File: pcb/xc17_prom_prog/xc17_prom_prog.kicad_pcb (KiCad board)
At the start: 2 copper layers, 123 x 95 mm, 288 parts, among them J1 Conn_02x02_Odd_Even, J2 USB_B_Micro, J3 Conn_02x20_Odd_Even, Q1 BC850, Q10 BC850, Q11 IRLML9301, Q12 IRLML9301, Q13 IRLML9301, Q14 IRLML9301, Q15 BC850, Q16 IRLML9301, Q17 IRLML9301, Q18 IRLML9301, Q19 IRLML9301, Q2 BC850, Q20 BC850, Q21 BC850, Q22 BC850, Q23 BC850, Q24 BC850, Q3 IRLML9301, Q4 IRLML9301, Q5 IRLML9301, Q6 BC850, Q7 IRLML9301, Q8 IRLML9301, Q9 BC850, U1 W25Q32JVSSIM, U10 LM317, U11 LM317, U12 LM317, U13 MC33063AD, U14 MC33063AD, U15 SN74LVC8T245, U16 SN74LVC8T245, U17 SN74LVC8T245, U18 XC17xxx, U2 LT3030, U3 ICE40HX1K-VQ100, U4 93LC56B, U5 FT2232HL, U6 LM317, U7 LM317, U8 LM317, U9 LM317, X1 12M

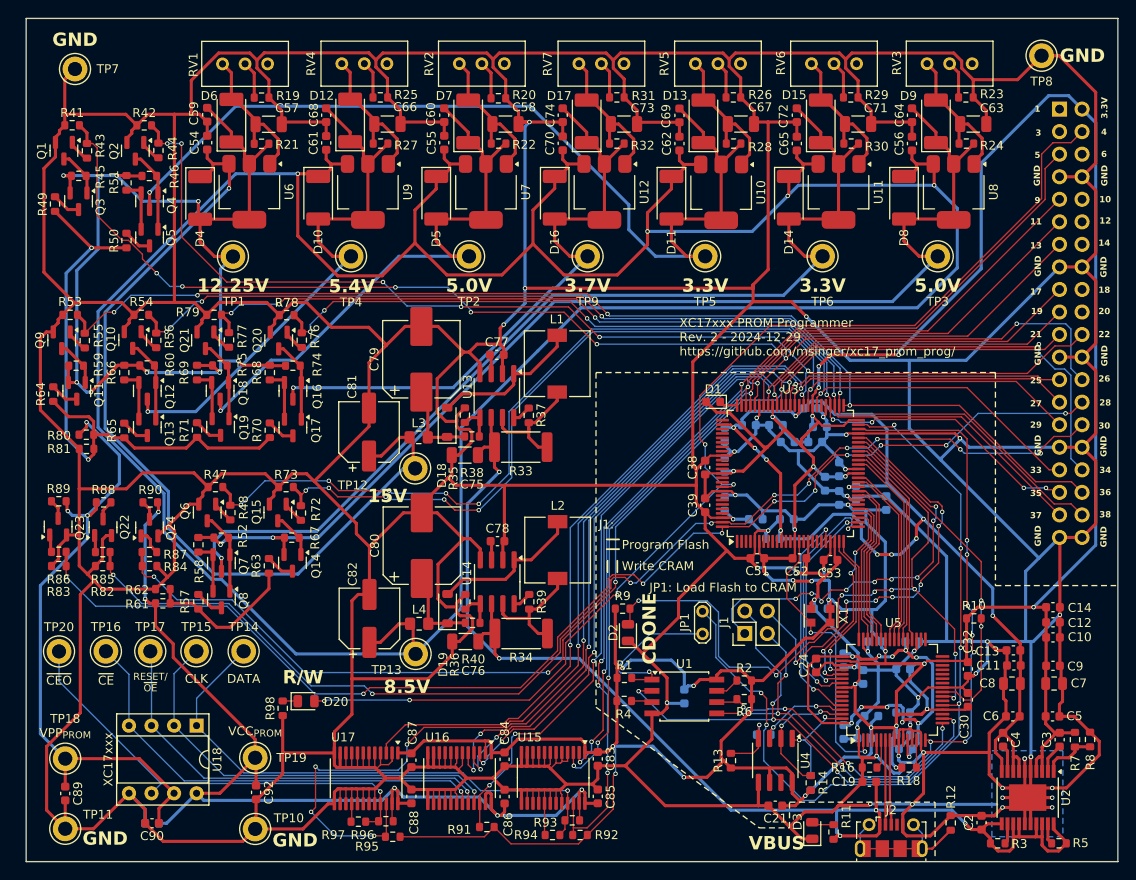
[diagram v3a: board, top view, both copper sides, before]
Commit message: Remove unused components
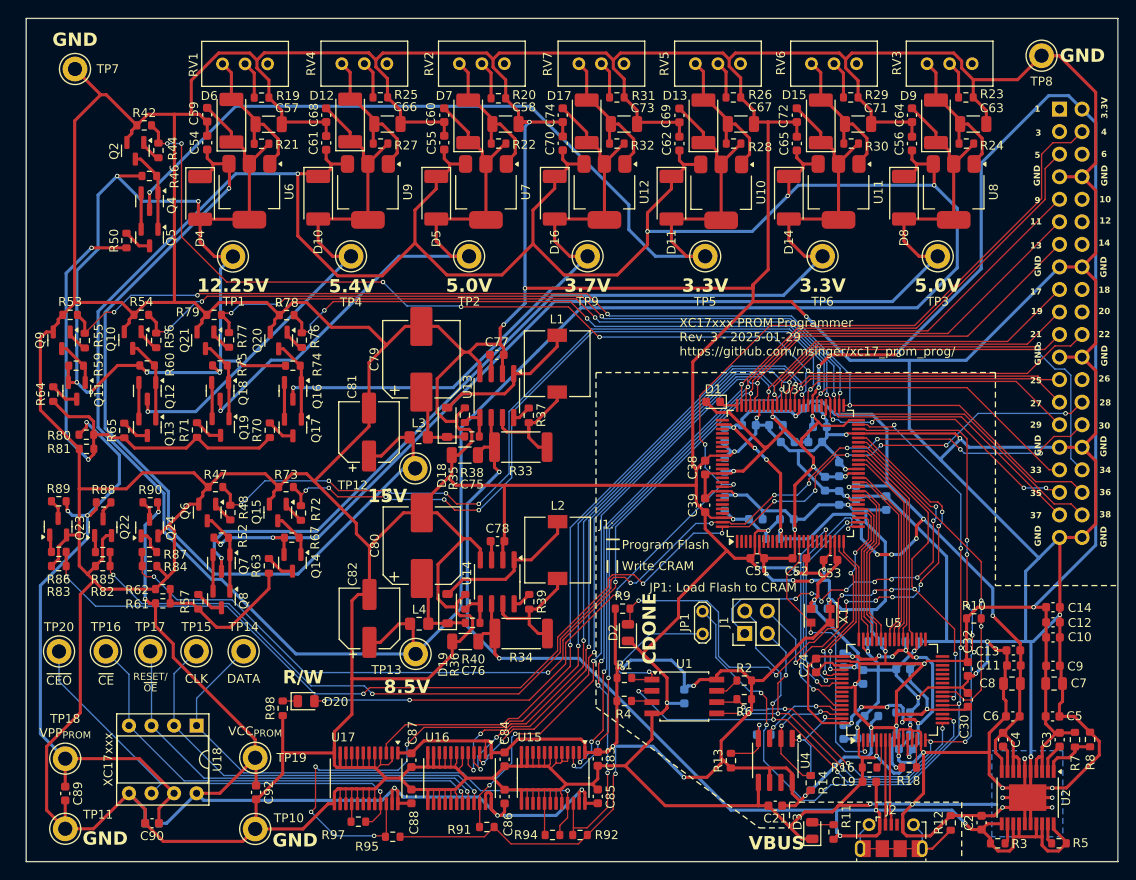
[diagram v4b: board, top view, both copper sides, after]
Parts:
- removed Q1: BC850, Package_TO_SOT_SMD:SOT-23
- removed Q3: IRLML9301, Package_TO_SOT_SMD:SOT-23
- removed R41: 10k, Resistor_SMD:R_0603_1608Metric
- removed R43: 422, Resistor_SMD:R_0603_1608Metric
- removed R45: 2.05k, Resistor_SMD:R_0603_1608Metric
- removed R49: 1.5, Resistor_SMD:R_0603_1608Metric
- removed R51, R58, R66, R68, R69: 1M, Resistor_SMD:R_0603_1608Metric
- removed R93, R96: 100k, Resistor_SMD:R_0603_1608Metric
- R64: value 0 -> 1.5
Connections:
- J3 pad 26: /FPGA/SELECT_VPP_12V25_WEAK -> unconnected-(J3-Pin_26-Pad26)
- U3 pad 69: /FPGA/SELECT_VPP_12V25_WEAK -> unconnected-(U3B-IOR_68-Pad69)
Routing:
- net /FPGA/SELECT_VPP_12V25_WEAK: track 142.6 -> 0.00 mm, vias 7 -> 0
- net +12V25P: track 124.4 -> 114.5 mm, vias 8 -> 7
- net Net-(R50-Pad2): track 67.8 -> 62.0 mm
- net Net-(Q1-C): track 5.25 -> 0.00 mm
- net VCC_{PROM}: track 119.4 -> 115.5 mm
- net GND: track 1606.1 -> 1602.5 mm
- net Net-(Q3-D): track 3.25 -> 0.00 mm
- net Net-(Q1-B): track 2.58 -> 0.00 mm
- net +5VC: track 131.1 -> 129.4 mm
- net Net-(Q4-S): track 5.84 -> 4.10 mm
- net Net-(Q16-S): track 5.85 -> 4.12 mm
- net Net-(Q18-S): track 5.78 -> 4.10 mm
- net Net-(Q12-S): track 5.78 -> 4.10 mm
- net Net-(Q7-S): track 5.73 -> 4.10 mm

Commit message: Migrate from HX1K to HX4K FPGA
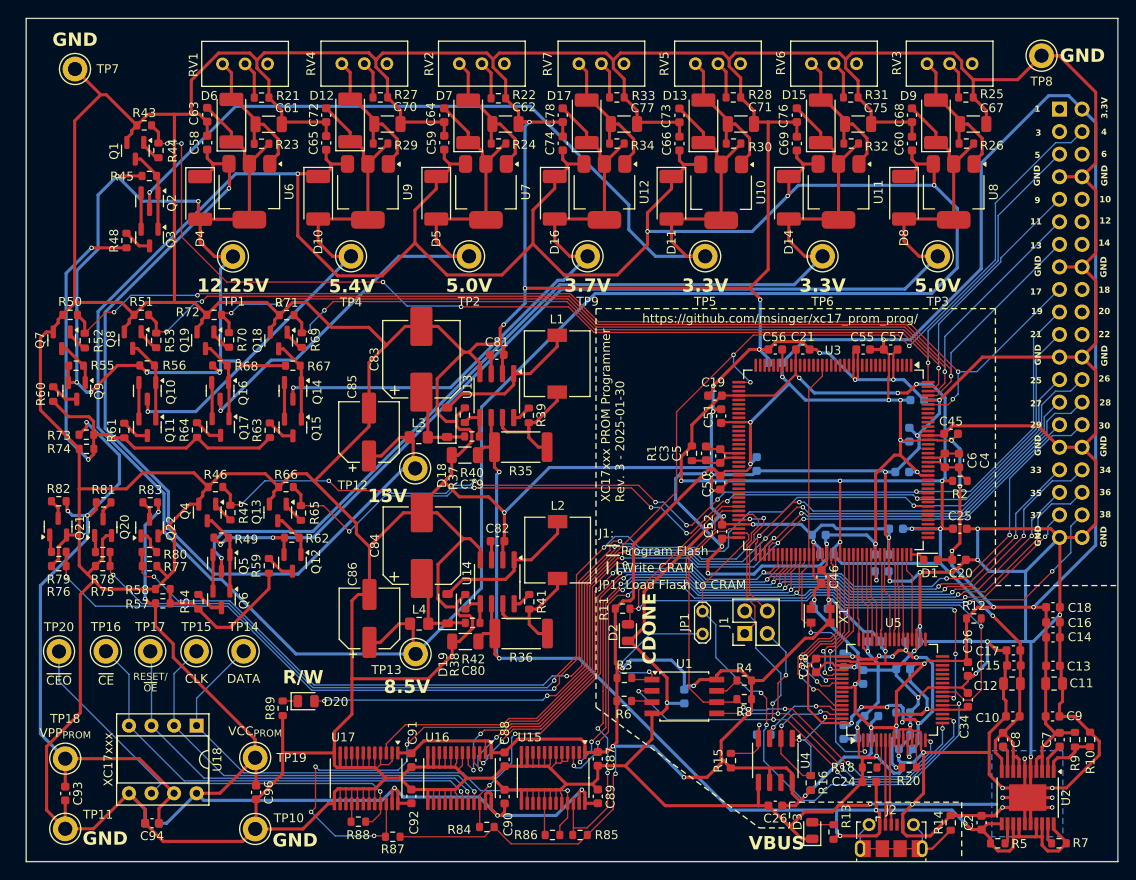
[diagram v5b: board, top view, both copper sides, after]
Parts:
- removed the C15 at (174.1, 98.6)
- removed the C16 at (175.7, 96.4)
- removed the C17 at (183.5, 93.5)
- removed the C18 at (178.4, 83.9)
- removed the C38 at (166.5, 90.6)
- removed the C39 at (166.5, 94.8)
- removed the C40 at (168.7, 90.3)
- removed the C41 at (168.7, 94.7)
- added C19: 100n, Capacitor_SMD:C_0603_1608Metric, F.Cu at (167.6, 82.5)
- added C21: 100n, Capacitor_SMD:C_0603_1608Metric, F.Cu at (177.5, 77.3)
- added C22: 100n, Capacitor_SMD:C_0603_1608Metric, B.Cu at (180.2, 100.4)
- added C25: 10n, Capacitor_SMD:C_0603_1608Metric, F.Cu at (195.2, 97.5)
- added C3: 10µ, Capacitor_SMD:C_0603_1608Metric, F.Cu at (166.6, 89.0)
- added C4: 10µ, Capacitor_SMD:C_0603_1608Metric, F.Cu at (195.1, 89.8)
- added C5: 100n, Capacitor_SMD:C_0603_1608Metric, F.Cu at (168.2, 89.3)
- added C54: 100n, Capacitor_SMD:C_0603_1608Metric, B.Cu at (174.4, 78.8)
- added C55: 100n, Capacitor_SMD:C_0603_1608Metric, F.Cu at (184.3, 77.3)
- added C56: 100n, Capacitor_SMD:C_0603_1608Metric, F.Cu at (174.4, 77.3)
- added C57: 100n, Capacitor_SMD:C_0603_1608Metric, F.Cu at (187.4, 77.3)
- added C6: 100n, Capacitor_SMD:C_0603_1608Metric, F.Cu at (193.5, 89.8)
- added R1: 100, Resistor_SMD:R_0603_1608Metric, F.Cu at (165.0, 89.0)
- added R2: 100, Resistor_SMD:R_0603_1608Metric, F.Cu at (195.2, 92.1)
- C20: value 100n -> 10n; moved to F.Cu
- C23: value 10n -> 100n
- C45, C46, C50: moved to F.Cu
- C53: moved to B.Cu
- U3: value ICE40HX1K-VQ100 -> ICE40HX4K-TQ144; footprint Package_QFP:VQFP-100_14x14mm_P0.5mm -> Package_QFP:TQFP-144_20x20mm_P0.5mm
- moved D1 30.3 mm to (191.9, 101.0), turned to 0 degrees
- moved C20 29.9 mm to (195.1, 101.0), turned to 0 degrees
- moved C23 20.3 mm to (188.0, 97.5), turned to 180 degrees
- moved C51 16.5 mm to (168.3, 84.8), turned to 90 degrees
- moved C45 15.3 mm to (194.2, 86.8), turned to 180 degrees
- moved C43 15.1 mm to (189.5, 86.9), turned to 90 degrees
- moved C53 13.7 mm to (172.3, 90.2), turned to -90 degrees
- moved C44 13.3 mm to (188.7, 91.1)
- moved C46 12.3 mm to (179.6, 102.9), turned to -90 degrees
- moved C48 11.8 mm to (186.4, 102.3), turned to 0 degrees
- moved C42 11.4 mm to (190.4, 83.0)
- moved C52 9.23 mm to (168.4, 97.8), turned to 90 degrees
- moved C49 5.82 mm to (186.4, 100.4), turned to 0 degrees
- moved C50 5.75 mm to (168.2, 92.3), turned to -90 degrees
- moved U3 5.08 mm to (180.9, 89.7), turned to -90 degrees
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- renumbered C6 to C10, C7 to C11, C8 to C12, C9 to C13, C10 to C14, C11 to C15, C12 to C16, C13 to C17, C14 to C18, C19 to C24, C21 to C26, C22 to C27, C24 to C28, C25 to C29, C26 to C30, C27 to C31, C28 to C32, C29 to C33, C30 to C34, C31 to C35, C32 to C36, C33 to C37, C34 to C38, C35 to C39, C36 to C40, C37 to C41, C54 to C58, C55 to C59, C56 to C60, C57 to C61, C58 to C62, C59 to C63, C60 to C64, C61 to C65, C62 to C66, C63 to C67, C64 to C68, C65 to C69, C3 to C7, C66 to C70, C67 to C71, C68 to C72, C69 to C73, C70 to C74, C71 to C75, C72 to C76, C73 to C77, C74 to C78, C75 to C79, C4 to C8, C76 to C80, C77 to C81, C78 to C82, C79 to C83, C80 to C84, C81 to C85, C82 to C86, C83 to C87, C84 to C88, C85 to C89, C5 to C9, C86 to C90, C87 to C91, C88 to C92, C89 to C93, C90 to C94, C91 to C95, C92 to C96, Q2 to Q1, Q12 to Q10, Q13 to Q11, Q14 to Q12, Q15 to Q13, Q16 to Q14, Q17 to Q15, Q18 to Q16, Q19 to Q17, Q20 to Q18, Q21 to Q19, Q4 to Q2, Q22 to Q20, Q23 to Q21, Q24 to Q22, Q5 to Q3, Q6 to Q4, Q7 to Q5, Q8 to Q6, Q9 to Q7, Q10 to Q8, Q11 to Q9, R8 to R10, R9 to R11, R10 to R12, R11 to R13, R12 to R14, R13 to R15, R14 to R16, R15 to R17, R16 to R18, R17 to R19, R18 to R20, R19 to R21, R20 to R22, R21 to R23, R22 to R24, R23 to R25, R24 to R26, R25 to R27, R26 to R28, R27 to R29, R1 to R3, R28 to R30, R29 to R31, R30 to R32, R31 to R33, R32 to R34, R33 to R35, R34 to R36, R35 to R37, R36 to R38, R37 to R39, R2 to R4, R38 to R40, R39 to R41, R40 to R42, R42 to R43, R46 to R45, R47 to R46, R48 to R47, R50 to R48, R52 to R49, R3 to R5, R53 to R50, R54 to R51, R55 to R52, R56 to R53, R57 to R54, R59 to R55, R60 to R56, R61 to R57, R62 to R58, R63 to R59, R4 to R6, R64 to R60, R65 to R61, R67 to R62, R70 to R63, R71 to R64, R72 to R65, R73 to R66, R74 to R67, R75 to R68, R76 to R69, R5 to R7, R77 to R70, R78 to R71, R79 to R72, R80 to R73, R81 to R74, R82 to R75, R83 to R76, R84 to R77, R85 to R78, R86 to R79, R6 to R8, R87 to R80, R88 to R81, R89 to R82, R90 to R83, R91 to R84, R92 to R85, R94 to R86, R95 to R87, R97 to R88, R98 to R89, R7 to R9
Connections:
- C20 pad 1: +1V2 -> +3V3
- J3 pad 11: /FPGA/PROM_DATA -> /FPGA/SELECT_VPP_5V
- J3 pad 13: /FPGA/CONTROL_~{OE} -> /FPGA/SELECT_VPP_5V4
- J3 pad 17: /FPGA/PROM_CLK -> /FPGA/SELECT_VPP_12V25
- J3 pad 19: /FPGA/PROM_RESET_~{OE} -> /FPGA/SELECT_VCC_3V3
- J3 pad 21: /FPGA/PROM_~{CE} -> /FPGA/SELECT_VCC_5V
- J3 pad 22: /FPGA/SELECT_VPP_3V3 -> unconnected-(J3-Pin_22-Pad22)
- J3 pad 25: /FPGA/~{CEO_OE} -> /FPGA/SELECT_VPP_GND
- J3 pad 26: unconnected-(J3-Pin_26-Pad26) -> /FPGA/SELECT_VPP_GND_WEAK
- J3 pad 27: /FPGA/PROM_~{CEO} -> /FPGA/SELECT_VCC_GND
- J3 pad 28: /FPGA/SELECT_VPP_GND_WEAK -> /FPGA/PROM_~{CEO}
- J3 pad 29: /FPGA/SELECT_VCC_5V -> /FPGA/~{CEO_OE}
- J3 pad 30: /FPGA/SELECT_VPP_GND -> /FPGA/PROM_~{CE}
- J3 pad 33: /FPGA/SELECT_VCC_3V3 -> /FPGA/PROM_RESET_~{OE}
- J3 pad 34: /FPGA/SELECT_VCC_GND -> /FPGA/PROM_CLK
- J3 pad 35: /FPGA/SELECT_VPP_3V7 -> /FPGA/CONTROL_~{OE}
- J3 pad 36: /FPGA/SELECT_VPP_12V25 -> /FPGA/DATA_~{OE}
- J3 pad 37: /FPGA/SELECT_VPP_5V -> /FPGA/DATA_DIR
- J3 pad 38: /FPGA/SELECT_VPP_5V4 -> /FPGA/PROM_DATA
- J3 pad 5: /FPGA/DATA_~{OE} -> /FPGA/SELECT_VPP_3V3
- J3 pad 9: /FPGA/DATA_DIR -> /FPGA/SELECT_VPP_3V7
- U3 pad 100: /FPGA/SELECT_VPP_GND_WEAK -> +3V3
- U3 pad 11: +1V2 -> unconnected-(U3D-IOL_8A-Pad11)
- U3 pad 13: unconnected-(U3D-IOL_6B_GBIN7-Pad13) -> GND
- U3 pad 14: +3V3 -> GND
- U3 pad 15: /FPGA Power/CLK12M -> unconnected-(U3D-IOL_10A-Pad15)
- U3 pad 17: GND -> unconnected-(U3D-IOL_12A-Pad17)
- U3 pad 21: /FPGA Power/USB_~{PWREN} -> /FPGA/CLK12M
- U3 pad 22: +3V3 -> unconnected-(U3D-IOL_14B-Pad22)
- U3 pad 23: GND -> unconnected-(U3D-IOL_17A-Pad23)
- U3 pad 24: /FPGA Power/CBUS1 -> unconnected-(U3D-IOL_17B-Pad24)
- U3 pad 25: /FPGA Power/CBUS0 -> unconnected-(U3D-IOL_18A-Pad25)
- U3 pad 26: /FPGA Power/CBUS4 -> unconnected-(U3D-IOL_18B-Pad26)
- U3 pad 27: /FPGA Power/CBUS3 -> +1V2
- U3 pad 28: /FPGA Power/CBUS2 -> unconnected-(U3D-IOL_23A-Pad28)
- U3 pad 29: /FPGA Power/DBUS7 -> unconnected-(U3D-IOL_23B-Pad29)
- U3 pad 30: /FPGA Power/DBUS6 -> +3V3
- U3 pad 31: +3V3 -> unconnected-(U3D-IOL_24A-Pad31)
- U3 pad 32: GND -> unconnected-(U3D-IOL_24B-Pad32)
- U3 pad 33: /FPGA Power/DBUS5 -> unconnected-(U3D-IOL_25A-Pad33)
- U3 pad 34: /FPGA Power/DBUS4 -> unconnected-(U3D-IOL_25B-Pad34)
- U3 pad 35: +1V2 -> unconnected-(U3E-NC-Pad35)
- U3 pad 36: /FPGA Power/DBUS3 -> unconnected-(U3E-NC-Pad36)
- U3 pad 37: /FPGA Power/DBUS2 -> /FPGA/PROM_LED
- U3 pad 38: +3V3 -> unconnected-(U3C-IOB_57-Pad38)
- U3 pad 39: GND -> unconnected-(U3C-IOB_61-Pad39)
- U3 pad 40: /FPGA Power/DBUS1 -> +1V2
- U3 pad 41: /FPGA Power/DBUS0 -> unconnected-(U3C-IOB_63-Pad41)
- U3 pad 42: /FPGA Power/USB_~{SUSPEND} -> unconnected-(U3C-IOB_64-Pad42)
- U3 pad 43: /FPGA Power/CDONE -> unconnected-(U3C-IOB_71-Pad43)
- U3 pad 44: /FPGA Power/~{CRESET} -> unconnected-(U3C-IOB_72-Pad44)
- U3 pad 45: Net-(J1-Pin_1) -> unconnected-(U3C-IOB_73-Pad45)
- U3 pad 46: Net-(J1-Pin_4) -> +3V3
- U3 pad 47: GND -> unconnected-(U3C-IOB_79-Pad47)
- U3 pad 48: /FPGA Power/SCK -> unconnected-(U3C-IOB_80-Pad48)
- U3 pad 49: /FPGA Power/SS -> unconnected-(U3C-IOB_81_GBIN5-Pad49)
- U3 pad 50: +3V3 -> unconnected-(U3E-NC-Pad50)
- U3 pad 51: /FPGA/SELECT_VPP_12V25 -> unconnected-(U3E-NC-Pad51)
- U3 pad 52: /FPGA/SELECT_VPP_5V4 -> unconnected-(U3C-IOB_82_GBIN4-Pad52)
- U3 pad 53: /FPGA/SELECT_VPP_5V -> Net-(U3E-GNDPLL0)
- U3 pad 54: /FPGA/SELECT_VPP_3V7 -> Net-(U3E-VCCPLL0)
- U3 pad 55: GND -> unconnected-(U3C-IOB_91-Pad55)
- U3 pad 57: /FPGA/SELECT_VCC_3V3 -> +3V3
- U3 pad 58: +3V3 -> unconnected-(U3E-NC-Pad58)
- U3 pad 59: /FPGA/SELECT_VCC_5V -> GND
- U3 pad 60: /FPGA/SELECT_VPP_3V3 -> unconnected-(U3C-IOB_95-Pad60)
- U3 pad 61: +1V2 -> unconnected-(U3C-IOB_96-Pad61)
- U3 pad 62: /FPGA/PROM_~{CEO} -> unconnected-(U3C-IOB_102-Pad62)
- U3 pad 63: /FPGA/~{CEO_OE} -> unconnected-(U3C-IOB_103_CBSEL0-Pad63)
- U3 pad 64: /FPGA/PROM_~{CE} -> unconnected-(U3C-IOB_104_CBSEL1-Pad64)
- U3 pad 65: /FPGA/SELECT_VCC_GND -> /FPGA Power/CDONE
- U3 pad 66: /FPGA/PROM_RESET_~{OE} -> /FPGA Power/~{CRESET}
- U3 pad 67: +3V3 -> Net-(J1-Pin_1)
- U3 pad 68: /FPGA/PROM_CLK -> Net-(J1-Pin_4)
- U3 pad 69: unconnected-(U3B-IOR_68-Pad69) -> GND
- U3 pad 70: GND -> /FPGA Power/SCK
- U3 pad 71: /FPGA/CONTROL_~{OE} -> /FPGA Power/SS
- U3 pad 72: /FPGA/PROM_DATA -> +3V3
- U3 pad 73: /FPGA/DATA_DIR -> /FPGA/SELECT_VPP_GND_WEAK
- U3 pad 74: /FPGA/DATA_~{OE} -> /FPGA/SELECT_VCC_GND
- U3 pad 75: Net-(D1-K) -> /FPGA/PROM_~{CEO}
- U3 pad 76: unconnected-(U3E-VPP_FAST-Pad76) -> /FPGA/~{CEO_OE}
- U3 pad 77: +1V2 -> unconnected-(U3E-NC-Pad77)
- U3 pad 78: unconnected-(U3A-IOT_73-Pad78) -> /FPGA/PROM_~{CE}
- U3 pad 79: unconnected-(U3A-IOT_74-Pad79) -> /FPGA/PROM_RESET_~{OE}
- U3 pad 80: unconnected-(U3A-IOT_75-Pad80) -> /FPGA/PROM_CLK
- U3 pad 81: unconnected-(U3A-IOT_77-Pad81) -> /FPGA/CONTROL_~{OE}
- U3 pad 82: unconnected-(U3A-IOT_78-Pad82) -> /FPGA/DATA_~{OE}
- U3 pad 83: unconnected-(U3A-IOT_79-Pad83) -> /FPGA/DATA_DIR
- U3 pad 84: GND -> /FPGA/PROM_DATA
- U3 pad 85: unconnected-(U3A-IOT_80-Pad85) -> /FPGA/CLK12M
- U3 pad 86: unconnected-(U3A-IOT_81-Pad86) -> GND
- U3 pad 88: +3V3 -> unconnected-(U3B-IOR_137-Pad88)
- U3 pad 89: unconnected-(U3A-IOT_84_GBIN1-Pad89) -> +3V3
- U3 pad 90: unconnected-(U3A-IOT_85_GBIN0-Pad90) -> /FPGA Power/USB_~{PWREN}
- U3 pad 91: /FPGA/PROM_LED -> /FPGA Power/CBUS4
- U3 pad 92: +3V3 -> +1V2
- U3 pad 93: unconnected-(U3A-IOT_87-Pad93) -> /FPGA Power/CBUS3
- U3 pad 94: unconnected-(U3A-IOT_88-Pad94) -> /FPGA Power/CBUS2
- U3 pad 95: unconnected-(U3A-IOT_89-Pad95) -> /FPGA Power/CBUS1
- U3 pad 96: unconnected-(U3A-IOT_90-Pad96) -> /FPGA Power/CBUS0
- U3 pad 97: unconnected-(U3A-IOT_91-Pad97) -> /FPGA Power/DBUS7
- U3 pad 98: GND -> /FPGA Power/DBUS6
- U3 pad 99: /FPGA/SELECT_VPP_GND -> /FPGA Power/DBUS5
- U5 pad 2: /FPGA Power/CLK12M -> /FPGA/CLK12M
- X1 pad 3: /FPGA Power/CLK12M -> /FPGA/CLK12M
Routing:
- net /FPGA/CLK12M: track 0.00 -> 51.8 mm, vias 0 -> 2
- net +3V3: track 531.4 -> 579.4 mm, vias 30 -> 33
- net +1V2: track 122.2 -> 158.8 mm, vias 11 -> 10
- net Net-(J1-Pin_4): track 49.1 -> 14.8 mm, vias 7 -> 2
- net /FPGA Power/CLK12M: track 31.9 -> 0.00 mm, vias 2 -> 0
- net Net-(J1-Pin_1): track 47.3 -> 16.7 mm, vias 9 -> 0
- net /FPGA Power/SS: track 91.8 -> 65.1 mm, vias 6 -> 3
- net /FPGA Power/SCK: track 82.5 -> 56.3 mm, vias 10 -> 4
- net /FPGA Power/~{CRESET}: track 39.8 -> 61.4 mm
- net /FPGA/DATA_DIR: track 97.6 -> 82.8 mm, vias 4 -> 6
- net /FPGA/DATA_~{OE}: track 114.2 -> 99.4 mm, vias 4 -> 6
- net /FPGA Power/CDONE: track 82.6 -> 68.4 mm, vias 8 -> 4
- net /FPGA Power/USB_~{SUSPEND}: track 23.7 -> 9.82 mm
- net /FPGA Power/DBUS0: track 23.1 -> 9.61 mm
- net /FPGA Power/DBUS1: track 22.6 -> 9.61 mm
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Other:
- board text added: "${COMMENT1}"
- board text added: "${TITLE} Rev. ${REVISION} - ${ISSUE_DATE}"
- board text removed: "${TITLE} Rev. ${REVISION} - ${ISSUE_DATE} ${COMMENT1}"
